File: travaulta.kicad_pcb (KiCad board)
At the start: 4 copper layers, 209.7 x 76.4 mm, 106 parts, among them SW1 EC_SW, SW10 EC_SW, SW11 EC_SW, SW12 EC_SW, SW13 EC_SW, SW14 EC_SW, SW15 EC_SW, SW16 EC_SW, SW17 EC_SW, SW18 EC_SW, SW19 EC_SW, SW2 EC_SW, SW20 EC_SW, SW21 EC_SW, SW22 EC_SW, SW23 EC_SW, SW24 EC_SW, SW25 EC_SW, SW26 EC_SW, SW27 EC_SW, SW28 EC_SW, SW29 EC_SW, SW3 EC_SW, SW30 EC_SW, SW31 EC_SW, SW32 EC_SW, SW33 EC_SW, SW34 EC_SW, SW35 EC_SW, SW36 EC_SW, SW37 EC_SW, SW38 BOOT0, SW4 EC_SW, SW5 EC_SW, SW6 EC_SW, SW7 EC_SW, SW8 EC_SW, SW9 EC_SW, U1 STM32F401CBUx, U2 XC6206PxxxMR, U3 74HC4051, U4 74HC4051, U5 OPA350, Y1 8 MHz

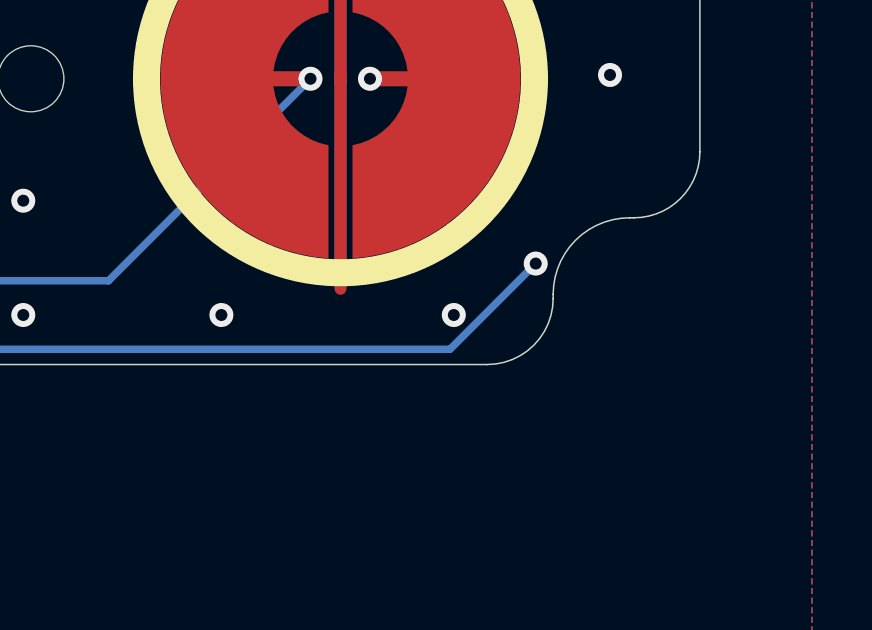
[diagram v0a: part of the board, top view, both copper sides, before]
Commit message: small schematic error fixed
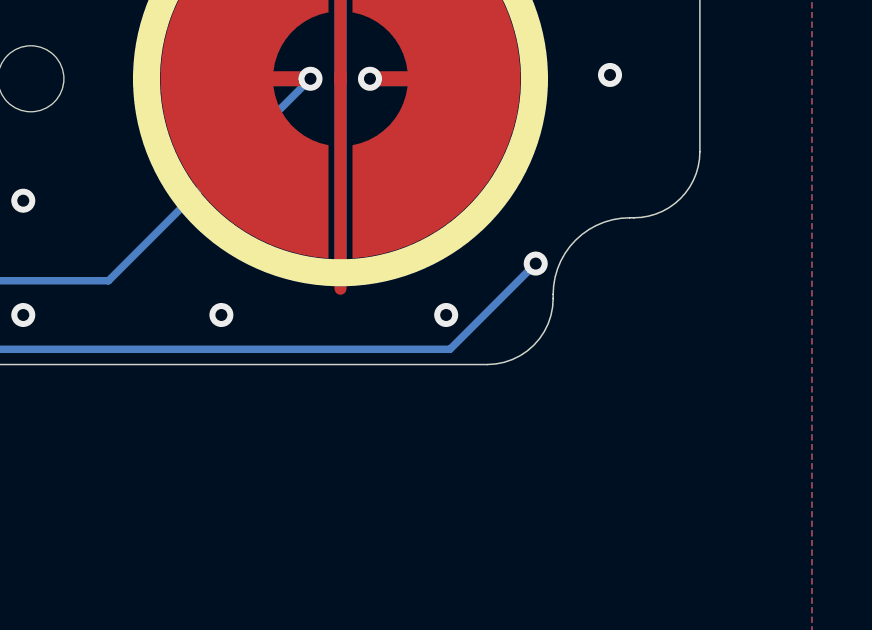
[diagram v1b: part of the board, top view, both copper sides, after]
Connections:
- SW11 pad 3: unconnected-(SW11-SG-Pad3) -> GND
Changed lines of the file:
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@@
   (net 62 "unconnected-(U1-PB7-Pad43)")
   (net 63 "COL10")
-  (net 64 "unconnected-(SW11-SG-Pad3)")
   (footprint "cipulot_parts:ecs_pad_1U_no_ring" locked (layer "F.Cu")
     (at 211.1375 76.2)
@@
       ))
     (pad "3" smd custom locked (at 0 0) (size 0.4 0.4) (layers "F.Cu")
-      (net 64 "unconnected-(SW11-SG-Pad3)") (pinfunction "SG") (pintype "input") (zone_connect 2) (thermal_bridge_angle 45)
+      (net 1 "GND") (pinfunction "SG") (pintype "input") (zone_connect 2) (thermal_bridge_angle 45)
       (options (clearance convexhull) (anchor rect))
       (primitives
@@
       ))
     (pad "3" smd custom locked (at 0 0) (size 0.4 0.4) (layers "B.Cu")
-      (net 64 "unconnected-(SW11-SG-Pad3)") (pinfunction "SG") (pintype "input") (zone_connect 2) (thermal_bridge_angle 45)
+      (net 1 "GND") (pinfunction "SG") (pintype "input") (zone_connect 2) (thermal_bridge_angle 45)
       (options (clearance convexhull) (anchor rect))
       (primitives
@@
   (via (at 144.460375 118.364) (size 0.8) (drill 0.4) (layers "F.Cu" "B.Cu") (net 1))
   (via (at 47.371 50.8) (size 0.8) (drill 0.4) (layers "F.Cu" "B.Cu") (free) (net 1))
-  (via (at 245.872 103.124) (size 0.8) (drill 0.4) (layers "F.Cu" "B.Cu") (net 1))
+  (via (at 245.618 103.124) (size 0.8) (drill 0.4) (layers "F.Cu" "B.Cu") (net 1))
   (via (at 99.695 65.786) (size 0.8) (drill 0.4) (layers "F.Cu" "B.Cu") (free) (net 1))
   (via (at 210.82 103.251) (size 0.8) (drill 0.4) (layers "F.Cu" "B.Cu") (net 1))

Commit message: backup
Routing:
- net GND: vias 275 -> 274
- net COL0: vias 4 -> 3
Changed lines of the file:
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@@
   (via (at 84.709 58.166) (size 0.8) (drill 0.4) (layers "F.Cu" "B.Cu") (free) (net 1))
   (via (at 141.859 72.517) (size 0.8) (drill 0.4) (layers "F.Cu" "B.Cu") (net 1))
-  (via (at 91.948 116.459) (size 0.8) (drill 0.4) (layers "F.Cu" "B.Cu") (net 1))
   (via (at 122.174 84.709) (size 0.8) (drill 0.4) (layers "F.Cu" "B.Cu") (free) (net 1))
   (via (at 68.453 76.2) (size 0.8) (drill 0.4) (layers "F.Cu" "B.Cu") (net 1))
@@
   (segment (start 143.827 86.36) (end 144.145 86.678) (width 0.2) (layer "B.Cu") (net 3))
   (segment (start 83.3 52.947) (end 83.3 53.624) (width 0.2) (layer "B.Cu") (net 3))
-  (segment (start 84.963 53.637) (end 84.95 53.624) (width 0.25) (layer "B.Cu") (net 4))
   (segment (start 84.95 52.870016) (end 84.95 53.624) (width 0.25) (layer "B.Cu") (net 4))
   (segment (start 80.15 57.8585) (end 80.9625 58.671) (width 0.25) (layer "B.Cu") (net 4))
@@
   (segment (start 146.742 111.127) (end 146.742 112.014) (width 0.25) (layer "B.Cu") (net 13))
   (via (at 62.103 95.25) (size 0.8) (drill 0.4) (layers "F.Cu" "B.Cu") (net 14))
-  (via (at 62.103 95.25) (size 0.8) (drill 0.4) (layers "F.Cu" "B.Cu") (net 14))
   (via (at 54.991 57.15) (size 0.8) (drill 0.4) (layers "F.Cu" "B.Cu") (net 14))
   (via (at 57.277 76.2) (size 0.8) (drill 0.4) (layers "F.Cu" "B.Cu") (net 14))
@@
   (via (at 226.441 57.15) (size 0.8) (drill 0.4) (layers "F.Cu" "B.Cu") (net 23))
   (via (at 236.347 76.2) (size 0.8) (drill 0.4) (layers "F.Cu" "B.Cu") (net 23))
-  (segment (start 241.095 95.25) (end 240.919 95.074) (width 0.5) (layer "In2.Cu") (net 23))
   (segment (start 232.918 63.627) (end 232.918 72.788) (width 0.5) (layer "In2.Cu") (net 23))
   (segment (start 241.095 95.25) (end 233.172 87.327) (width 0.5) (layer "In2.Cu") (net 23))
@@
   (segment (start 201.81316 122.29084) (end 201.81316 108.6358) (width 0.25) (layer "B.Cu") (net 43))
   (segment (start 158.5835 123.444) (end 200.66 123.444) (width 0.25) (layer "B.Cu") (net 43))
+  (segment (start 156.944 111.153) (end 157.353 110.744) (width 0.25) (layer "B.Cu") (net 43))
+  (segment (start 89.9 108.95) (end 89.9 115.672792) (width 0.25) (layer "B.Cu") (net 43))
   (segment (start 156.1225 123.444) (end 157.353 122.2135) (width 0.25) (layer "B.Cu") (net 43))
-  (segment (start 156.944 111.153) (end 157.353 110.744) (width 0.25) (layer "B.Cu") (net 43))
   (segment (start 157.353 122.2135) (end 158.5835 123.444) (width 0.25) (layer "B.Cu") (net 43))
-  (segment (start 89.9 116.31297) (end 97.031029 123.444) (width 0.25) (layer "B.Cu") (net 43))
-  (segment (start 89.9 108.95) (end 89.9 116.31297) (width 0.25) (layer "B.Cu") (net 43))
+  (segment (start 89.9 115.672792) (end 97.671208 123.444) (width 0.25) (layer "B.Cu") (net 43))
   (segment (start 156.944 111.153) (end 156.0915 111.153) (width 0.25) (layer "B.Cu") (net 43))
   (segment (start 156.0835 111.153) (end 156.944 111.153) (width 0.25) (layer "B.Cu") (net 43))
-  (segment (start 97.031029 123.444) (end 156.1225 123.444) (width 0.25) (layer "B.Cu") (net 43))
   (segment (start 89.5858 108.6358) (end 89.9 108.95) (width 0.25) (layer "B.Cu") (net 43))
   (segment (start 89.10066 108.6358) (end 89.5858 108.6358) (width 0.25) (layer "B.Cu") (net 43))
+  (segment (start 97.671208 123.444) (end 156.1225 123.444) (width 0.25) (layer "B.Cu") (net 43))
   (segment (start 157.353 121.162299) (end 158.078 120.437299) (width 0.25) (layer "F.Cu") (net 44))
   (segment (start 158.078 120.437299) (end 158.078 112.476402) (width 0.25) (layer "F.Cu") (net 44))
@@
   (via (at 157.353 121.162299) (size 0.8) (drill 0.4) (layers "F.Cu" "B.Cu") (net 44))
   (segment (start 159.189 122.994) (end 185.743 122.994) (width 0.25) (layer "B.Cu") (net 44))
+  (segment (start 90.35 115.486396) (end 97.857604 122.994) (width 0.25) (layer "B.Cu") (net 44))
+  (segment (start 155.521299 122.994) (end 157.353 121.162299) (width 0.25) (layer "B.Cu") (net 44))
   (segment (start 157.357299 111.755701) (end 157.254598 111.653) (width 0.25) (layer "B.Cu") (net 44))
-  (segment (start 97.217425 122.994) (end 155.521299 122.994) (width 0.25) (layer "B.Cu") (net 44))
   (segment (start 157.353 121.162299) (end 157.357299 121.162299) (width 0.25) (layer "B.Cu") (net 44))
-  (segment (start 90.35 116.126575) (end 97.217425 122.994) (width 0.25) (layer "B.Cu") (net 44))
+  (segment (start 90.23966 107.98556) (end 90.35 108.0959) (width 0.25) (layer "B.Cu") (net 44))
   (segment (start 89.10066 107.98556) (end 90.23966 107.98556) (width 0.25) (layer "B.Cu") (net 44))
-  (segment (start 90.23966 107.98556) (end 90.35 108.0959) (width 0.25) (layer "B.Cu") (net 44))
   (segment (start 198.84856 107.98556) (end 201.81316 107.98556) (width 0.25) (layer "B.Cu") (net 44))
   (segment (start 185.743 122.994) (end 187.452 121.285) (width 0.25) (layer "B.Cu") (net 44))
@@
   (segment (start 187.452 121.285) (end 187.452 109.18) (width 0.25) (layer "B.Cu") (net 44))
   (segment (start 157.357299 121.162299) (end 159.189 122.994) (width 0.25) (layer "B.Cu") (net 44))
-  (segment (start 155.521299 122.994) (end 157.353 121.162299) (width 0.25) (layer "B.Cu") (net 44))
   (segment (start 187.452 109.18) (end 189.629 107.003) (width 0.25) (layer "B.Cu") (net 44))
   (segment (start 197.866 107.003) (end 198.84856 107.98556) (width 0.25) (layer "B.Cu") (net 44))
-  (segment (start 90.35 108.0959) (end 90.35 116.126575) (width 0.25) (layer "B.Cu") (net 44))
+  (segment (start 97.857604 122.994) (end 155.521299 122.994) (width 0.25) (layer "B.Cu") (net 44))
   (segment (start 156.0835 111.653) (end 157.254598 111.653) (width 0.25) (layer "B.Cu") (net 44))
   (segment (start 189.629 107.003) (end 197.866 107.003) (width 0.25) (layer "B.Cu") (net 44))
+  (segment (start 90.35 108.0959) (end 90.35 115.486396) (width 0.25) (layer "B.Cu") (net 44))
   (segment (start 157.353 120.015) (end 157.628 119.74) (width 0.25) (layer "F.Cu") (net 45))
   (segment (start 157.628 119.74) (end 157.628 113.051) (width 0.25) (layer "F.Cu") (net 45))
@@
   (via (at 157.353 120.015) (size 0.8) (drill 0.4) (layers "F.Cu" "B.Cu") (net 45))
   (segment (start 155.508997 121.980997) (end 157.353 120.136994) (width 0.25) (layer "B.Cu") (net 45))
+  (segment (start 154.945994 122.544) (end 155.508997 121.980997) (width 0.25) (layer "B.Cu") (net 45))
   (segment (start 156.0835 112.153) (end 156.73 112.153) (width 0.25) (layer "B.Cu") (net 45))
   (segment (start 189.442604 106.553) (end 198.12 106.553) (width 0.25) (layer "B.Cu") (net 45))
-  (segment (start 93.8 118.940179) (end 97.403821 122.544) (width 0.25) (layer "B.Cu") (net 45))
   (segment (start 159.760006 122.544) (end 157.353 120.136994) (width 0.25) (layer "B.Cu") (net 45))
+  (segment (start 89.10066 107.33532) (end 90.23966 107.33532) (width 0.25) (layer "B.Cu") (net 45))
+  (segment (start 93.8 110.89566) (end 93.8 118.3) (width 0.25) (layer "B.Cu") (net 45))
   (segment (start 198.12 106.553) (end 198.90232 107.33532) (width 0.25) (layer "B.Cu") (net 45))
-  (segment (start 90.23966 107.33532) (end 93.8 110.89566) (width 0.25) (layer "B.Cu") (net 45))
   (segment (start 187.002 121.098604) (end 187.002 108.993604) (width 0.25) (layer "B.Cu") (net 45))
   (segment (start 157.358006 120.142) (end 159.760006 122.544) (width 0.25) (layer "B.Cu") (net 45))
-  (segment (start 93.8 110.89566) (end 93.8 118.940179) (width 0.25) (layer "B.Cu") (net 45))
+  (segment (start 93.8 118.3) (end 98.044 122.544) (width 0.25) (layer "B.Cu") (net 45))
+  (segment (start 90.23966 107.33532) (end 93.8 110.89566) (width 0.25) (layer "B.Cu") (net 45))
   (segment (start 198.90232 107.33532) (end 201.81316 107.33532) (width 0.25) (layer "B.Cu") (net 45))
   (segment (start 159.760006 122.544) (end 185.556604 122.544) (width 0.25) (layer "B.Cu") (net 45))
-  (segment (start 89.10066 107.33532) (end 90.23966 107.33532) (width 0.25) (layer "B.Cu") (net 45))
   (segment (start 157.347994 120.142) (end 157.353 120.142) (width 0.25) (layer "B.Cu") (net 45))
-  (segment (start 154.945994 122.544) (end 155.508997 121.980997) (width 0.25) (layer "B.Cu") (net 45))
   (segment (start 157.353 112.776) (end 156.73 112.153) (width 0.25) (layer "B.Cu") (net 45))
+  (segment (start 98.044 122.544) (end 154.945994 122.544) (width 0.25) (layer "B.Cu") (net 45))
   (segment (start 155.508997 121.980997) (end 157.347994 120.142) (width 0.25) (layer "B.Cu") (net 45))
   (segment (start 185.556604 122.544) (end 187.002 121.098604) (width 0.25) (layer "B.Cu") (net 45))
   (segment (start 187.002 108.993604) (end 189.442604 106.553) (width 0.25) (layer "B.Cu") (net 45))
-  (segment (start 97.403821 122.544) (end 154.945994 122.544) (width 0.25) (layer "B.Cu") (net 45))
   (segment (start 157.353 120.136994) (end 157.353 120.015) (width 0.25) (layer "B.Cu") (net 45))
   (segment (start 156.73 112.153) (end 156.0915 112.153) (width 0.25) (layer "B.Cu") (net 45))
@@
   (segment (start 247.8405 59.4995) (end 245.491 57.15) (width 0.5) (layer "In2.Cu") (net 63))
   (segment (start 247.8405 59.4995) (end 249.428 61.087) (width 0.5) (layer "In2.Cu") (net 63))
-  (segment (start 248.031 59.69) (end 247.8405 59.4995) (width 0.5) (layer "In2.Cu") (net 63))
   (segment (start 225.552 104.267) (end 245.745 104.267) (width 0.25) (layer "B.Cu") (net 63))
   (segment (start 223.141 106.678) (end 225.552 104.267) (width 0.25) (layer "B.Cu") (net 63))

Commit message: revision started
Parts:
- moved R24 0.54 mm to (84.2, 55.8)
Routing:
- net GND: track 41.9 -> 40.4 mm
- net Net-(USB1-CC2): track 2.30 -> 1.75 mm
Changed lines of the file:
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@@
   )
   (footprint "Resistor_SMD:R_0402_1005Metric" (layer "B.Cu")
-    (at 81.28 55.88 90)
+    (at 81.28 55.84625 90)
     (descr "Resistor SMD 0402 (1005 Metric), square (rectangular) end terminal, IPC_7351 nominal, (Body size source: IPC-SM-782 page 72, https://www.pcb-3d.com/wordpress/wp-content/uploads/ipc-sm-782a_amendment_1_and_2.pdf), generated with kicad-footprint-generator")
     (tags "resistor")
@@
   )
   (footprint "Resistor_SMD:R_0402_1005Metric" (layer "B.Cu")
-    (at 84.201 56.39 -90)
+    (at 84.201 55.84625 -90)
     (descr "Resistor SMD 0402 (1005 Metric), square (rectangular) end terminal, IPC_7351 nominal, (Body size source: IPC-SM-782 page 72, https://www.pcb-3d.com/wordpress/wp-content/uploads/ipc-sm-782a_amendment_1_and_2.pdf), generated with kicad-footprint-generator")
     (tags "resistor")
@@
     (effects (font (size 0.8 0.8) (thickness 0.15)) (justify mirror))
   )
-  (segment (start 81.28 57.277) (end 83.82 57.277) (width 0.25) (layer "F.Cu") (net 1))
-  (segment (start 83.82 57.277) (end 84.709 58.166) (width 0.25) (layer "F.Cu") (net 1))
+  (segment (start 84.188822 57.277) (end 84.198075 57.286253) (width 0.25) (layer "F.Cu") (net 1))
+  (segment (start 81.28 57.277) (end 84.188822 57.277) (width 0.25) (layer "F.Cu") (net 1))
   (via (at 74.295 91.313) (size 0.8) (drill 0.4) (layers "F.Cu" "B.Cu") (net 1))
   (via (at 188.214 122.174) (size 0.8) (drill 0.4) (layers "F.Cu" "B.Cu") (net 1))
@@
   (via (at 112.268 107.315) (size 0.8) (drill 0.4) (layers "F.Cu" "B.Cu") (net 1))
   (via (at 232.156 86.741) (size 0.8) (drill 0.4) (layers "F.Cu" "B.Cu") (free) (net 1))
+  (via (at 84.198075 57.286253) (size 0.8) (drill 0.4) (layers "F.Cu" "B.Cu") (net 1))
   (via (at 182.499 80.01) (size 0.8) (drill 0.4) (layers "F.Cu" "B.Cu") (net 1))
   (via (at 77.343 105.791) (size 0.8) (drill 0.4) (layers "F.Cu" "B.Cu") (free) (net 1))
@@
   (via (at 209.804 108.712) (size 0.8) (drill 0.4) (layers "F.Cu" "B.Cu") (net 1))
   (via (at 86.741 106.299) (size 0.8) (drill 0.4) (layers "F.Cu" "B.Cu") (net 1))
-  (via (at 84.709 58.166) (size 0.8) (drill 0.4) (layers "F.Cu" "B.Cu") (free) (net 1))
   (via (at 141.859 72.517) (size 0.8) (drill 0.4) (layers "F.Cu" "B.Cu") (net 1))
   (via (at 122.174 84.709) (size 0.8) (drill 0.4) (layers "F.Cu" "B.Cu") (free) (net 1))
@@
   (segment (start 78.29 53.624) (end 77.43 52.764) (width 0.25) (layer "B.Cu") (net 1))
   (segment (start 149.04 118.491) (end 149.031 118.5) (width 0.25) (layer "B.Cu") (net 1))
-  (segment (start 84.709 57.408) (end 84.709 58.166) (width 0.25) (layer "B.Cu") (net 1))
   (segment (start 82.903 69.85) (end 84.074 69.85) (width 0.25) (layer "B.Cu") (net 1))
   (segment (start 154.889279 109.405399) (end 154.889279 110.592899) (width 0.25) (layer "B.Cu") (net 1))
   (segment (start 152.646 112.903) (end 152.637137 112.903) (width 0.25) (layer "B.Cu") (net 1))
-  (segment (start 84.201 56.9) (end 84.709 57.408) (width 0.25) (layer "B.Cu") (net 1))
   (segment (start 89.377 48.864) (end 89.408 48.895) (width 0.25) (layer "B.Cu") (net 1))
   (segment (start 81.28 56.39) (end 81.28 57.277) (width 0.25) (layer "B.Cu") (net 1))
   (segment (start 75.723 48.864) (end 75.692 48.895) (width 0.25) (layer "B.Cu") (net 1))
+  (segment (start 84.201 56.35625) (end 84.201 57.283328) (width 0.25) (layer "B.Cu") (net 1))
   (segment (start 150.4001 110.665963) (end 150.5501 110.815963) (width 0.25) (layer "B.Cu") (net 1))
   (segment (start 77.43 51.094) (end 77.47 51.054) (width 0.25) (layer "B.Cu") (net 1))
@@
   (segment (start 158.299 114.935) (end 158.047 114.683) (width 0.25) (layer "B.Cu") (net 1))
   (segment (start 149.2126 110.665963) (end 150.4001 110.665963) (width 0.25) (layer "B.Cu") (net 1))
+  (segment (start 84.201 57.283328) (end 84.198075 57.286253) (width 0.25) (layer "B.Cu") (net 1))
   (segment (start 150.387137 110.653) (end 149.2165 110.653) (width 0.25) (layer "B.Cu") (net 1))
   (segment (start 153.396 109.4575) (end 153.404 109.4655) (width 0.2) (layer "B.Cu") (net 2))
@@
   (segment (start 81.28 53.644) (end 81.3 53.624) (width 0.25) (layer "B.Cu") (net 33))
   (segment (start 81.28 55.37) (end 81.28 53.644) (width 0.25) (layer "B.Cu") (net 33))
-  (segment (start 84.201 55.88) (end 84.201 53.723) (width 0.25) (layer "B.Cu") (net 34))
-  (segment (start 84.201 53.723) (end 84.3 53.624) (width 0.25) (layer "B.Cu") (net 34))
+  (segment (start 84.3 55.23725) (end 84.201 55.33625) (width 0.25) (layer "B.Cu") (net 34))
+  (segment (start 84.3 53.624) (end 84.3 55.23725) (width 0.25) (layer "B.Cu") (net 34))
   (segment (start 148.235375 117.448625) (end 147.955 117.729) (width 0.25) (layer "B.Cu") (net 41))
   (segment (start 143.381624 120.906) (end 146.558624 117.729) (width 0.25) (layer "B.Cu") (net 41))
